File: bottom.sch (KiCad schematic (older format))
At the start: 8 parts, among them J6 FFC-0.5MM-6POS, J7 Port_3, J8 Port_4

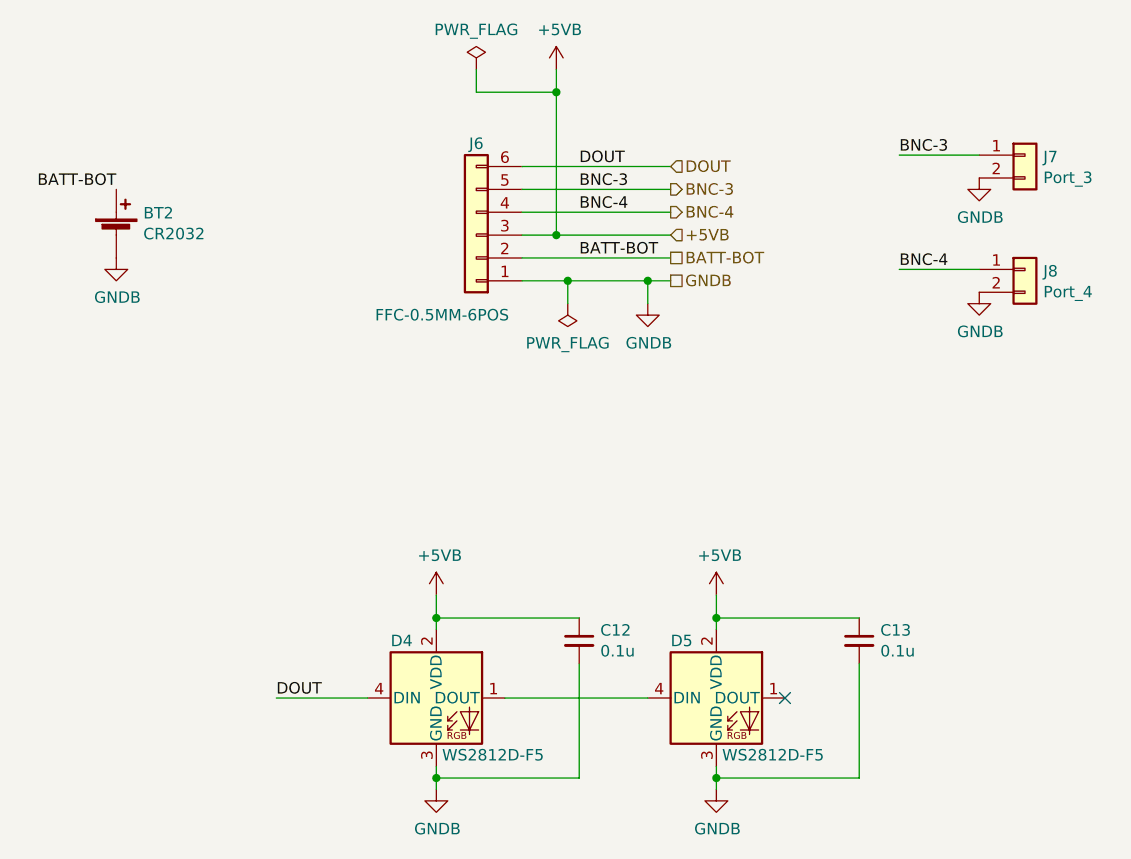
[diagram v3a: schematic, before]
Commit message: Fix: bottom FFC connector has wrong pinout
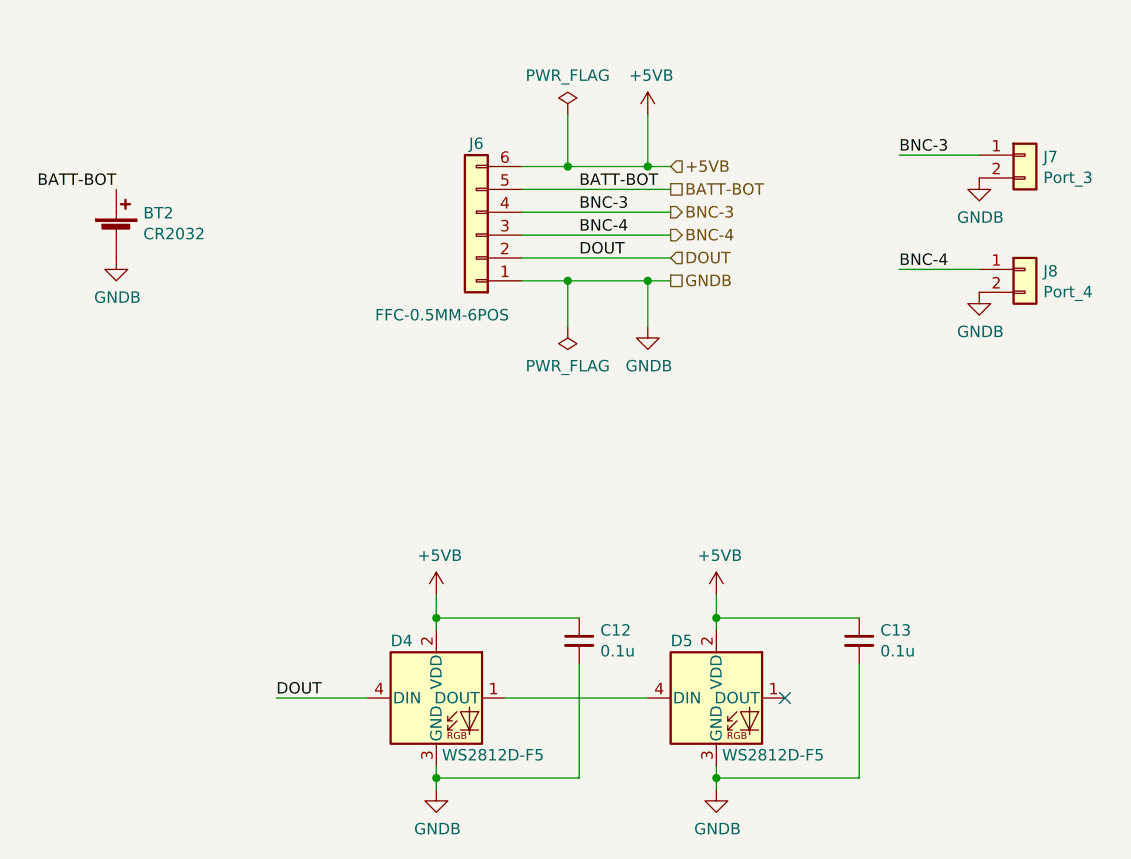
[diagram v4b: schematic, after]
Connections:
- net +5VB: now also J6.6 (Pin_6); no longer J6.3 (Pin_3)
- net BATT-BOT: now also J6.5 (Pin_5); no longer J6.2 (Pin_2)
- net BNC-3: now also J6.4 (Pin_4); no longer J6.5 (Pin_5)
- net BNC-4: now also J6.3 (Pin_3); no longer J6.4 (Pin_4)
- net DOUT: now also J6.2 (Pin_2); no longer J6.6 (Pin_6)
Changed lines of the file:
@@
 	1    0    0    -1
 $EndComp
-Text HLabel 5700 1925 2    50   Input ~ 0
-DOUT
-Text HLabel 5700 2025 2    50   Output ~ 0
-BNC-3
-Text HLabel 5700 2125 2    50   Output ~ 0
-BNC-4
-Text HLabel 5700 2325 2    50   UnSpc ~ 0
-BATT-BOT
-Text HLabel 5700 2425 2    50   UnSpc ~ 0
-GNDB
 Text Label 3275 2025 2    50   ~ 0
-BATT-BOT
-Text Label 5300 2325 0    50   ~ 0
 BATT-BOT
 $Comp
@@
 	1    0    0    -1
 $EndComp
-Text Label 5300 2125 0    50   ~ 0
-BNC-4
-Text Label 5300 2025 0    50   ~ 0
-BNC-3
-Text Label 5300 1925 0    50   ~ 0
-DOUT
 $Comp
 L Connector_Generic:Conn_01x06 J6
@@
 	-1   0    0    1
 $EndComp
-Wire Wire Line
-	5050 1925 5700 1925
-Wire Wire Line
-	5050 2025 5700 2025
-Wire Wire Line
-	5050 2125 5700 2125
-Wire Wire Line
-	5050 2325 5700 2325
 Text Label 6700 1875 0    50   ~ 0
 BNC-3
@@
 $EndComp
 $Comp
-L node:GNDB #PWR0103
-U 1 1 5CA43459
-P 5600 2525
-F 0 "#PWR0103" H 5600 2275 50  0001 C CNN
-F 1 "GNDB" H 5605 2352 50  0000 C CNN
-F 2 "" H 5600 2525 50  0001 C CNN
-F 3 "" H 5600 2525 50  0001 C CNN
-	1    5600 2525
-	1    0    0    -1
-$EndComp
-$Comp
 L node:GNDB #PWR0104
 U 1 1 5CA437BD
@@
 	1    0    0    -1
 $EndComp
-Text HLabel 5700 2225 2    50   Input ~ 0
-+5VB
 $Comp
 L node:+5VB #PWR0108
@@
 $EndComp
 $Comp
-L node:+5VB #PWR0110
-U 1 1 5CA4532B
-P 5200 1500
-F 0 "#PWR0110" H 5200 1350 50  0001 C CNN
-F 1 "+5VB" H 5215 1673 50  0000 C CNN
-F 2 "" H 5200 1500 50  0001 C CNN
-F 3 "" H 5200 1500 50  0001 C CNN
-	1    5200 1500
-	1    0    0    -1
-$EndComp
-$Comp
 L node:+5VB #PWR0109
 U 1 1 5CA03EDF
@@
 $EndComp
 Wire Wire Line
-	5200 2225 5700 2225
-Wire Wire Line
-	5050 2225 5200 2225
-Connection ~ 5200 2225
-Wire Wire Line
-	5200 1500 5200 1600
-Wire Wire Line
 	4675 3800 4675 3900
 Connection ~ 4675 3900
 Wire Wire Line
+	5250 2425 5600 2425
+Connection ~ 5250 2425
+Wire Wire Line
+	5250 2625 5250 2425
+$Comp
+L power:PWR_FLAG #FLG0102
+U 1 1 5CA09F39
+P 5250 2625
+F 0 "#FLG0102" H 5250 2700 50  0001 C CNN
+F 1 "PWR_FLAG" H 5250 2798 50  0000 C CNN
+F 2 "" H 5250 2625 50  0001 C CNN
+F 3 "~" H 5250 2625 50  0001 C CNN
+	1    5250 2625
+	-1   0    0    1
+$EndComp
+Wire Wire Line
+	5600 2425 5700 2425
+Connection ~ 5600 2425
+Wire Wire Line
+	5600 2625 5600 2425
+Wire Wire Line
 	5050 2425 5250 2425
-Wire Wire Line
-	5600 2525 5600 2425
-Connection ~ 5600 2425
-Wire Wire Line
-	5600 2425 5700 2425
+$Comp
+L node:GNDB #PWR0103
+U 1 1 5CA43459
+P 5600 2625
+F 0 "#PWR0103" H 5600 2375 50  0001 C CNN
+F 1 "GNDB" H 5605 2452 50  0000 C CNN
+F 2 "" H 5600 2625 50  0001 C CNN
+F 3 "" H 5600 2625 50  0001 C CNN
+	1    5600 2625
+	1    0    0    -1
+$EndComp
+Text HLabel 5700 2425 2    50   UnSpc ~ 0
+GNDB
+Text HLabel 5700 1925 2    50   Input ~ 0
++5VB
+Text HLabel 5700 2325 2    50   Input ~ 0
+DOUT
+Text HLabel 5700 2125 2    50   Output ~ 0
+BNC-3
+Text HLabel 5700 2225 2    50   Output ~ 0
+BNC-4
+Text HLabel 5700 2025 2    50   UnSpc ~ 0
+BATT-BOT
+Text Label 5300 2025 0    50   ~ 0
+BATT-BOT
+Text Label 5300 2225 0    50   ~ 0
+BNC-4
+Text Label 5300 2125 0    50   ~ 0
+BNC-3
+Text Label 5300 2325 0    50   ~ 0
+DOUT
+Wire Wire Line
+	5050 2325 5700 2325
+Wire Wire Line
+	5050 2125 5700 2125
+Wire Wire Line
+	5050 2225 5700 2225
+Wire Wire Line
+	5050 2025 5700 2025
+$Comp
+L node:+5VB #PWR0110
+U 1 1 5CA4532B
+P 5600 1700
+F 0 "#PWR0110" H 5600 1550 50  0001 C CNN
+F 1 "+5VB" H 5615 1873 50  0000 C CNN
+F 2 "" H 5600 1700 50  0001 C CNN
+F 3 "" H 5600 1700 50  0001 C CNN
+	1    5600 1700
+	1    0    0    -1
+$EndComp
 $Comp
 L power:PWR_FLAG #FLG0101
 U 1 1 5CA08161
-P 4850 1500
-F 0 "#FLG0101" H 4850 1575 50  0001 C CNN
-F 1 "PWR_FLAG" H 4850 1673 50  0000 C CNN
-F 2 "" H 4850 1500 50  0001 C CNN
-F 3 "~" H 4850 1500 50  0001 C CNN
-	1    4850 1500
-	1    0    0    -1
-$EndComp
-Wire Wire Line
-	4850 1500 4850 1600
-Wire Wire Line
-	4850 1600 5200 1600
-Connection ~ 5200 1600
-Wire Wire Line
-	5200 1600 5200 2225
-$Comp
-L power:PWR_FLAG #FLG0102
-U 1 1 5CA09F39
-P 5250 2525
-F 0 "#FLG0102" H 5250 2600 50  0001 C CNN
-F 1 "PWR_FLAG" H 5250 2698 50  0000 C CNN
-F 2 "" H 5250 2525 50  0001 C CNN
-F 3 "~" H 5250 2525 50  0001 C CNN
-	1    5250 2525
-	-1   0    0    1
-$EndComp
-Wire Wire Line
-	5250 2525 5250 2425
-Connection ~ 5250 2425
-Wire Wire Line
-	5250 2425 5600 2425
+P 5250 1700
+F 0 "#FLG0101" H 5250 1775 50  0001 C CNN
+F 1 "PWR_FLAG" H 5250 1873 50  0000 C CNN
+F 2 "" H 5250 1700 50  0001 C CNN
+F 3 "~" H 5250 1700 50  0001 C CNN
+	1    5250 1700
+	1    0    0    -1
+$EndComp
+Wire Wire Line
+	5600 1700 5600 1925
+Connection ~ 5600 1925
+Wire Wire Line
+	5600 1925 5700 1925
+Wire Wire Line
+	5050 1925 5250 1925
+Wire Wire Line
+	5250 1700 5250 1925
+Connection ~ 5250 1925
+Wire Wire Line
+	5250 1925 5600 1925
 $EndSCHEMATC

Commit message: Update entries for Seeed BOM
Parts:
- BT2: MPN BK-912 -> (none)
- J7, J8: MPN (none) -> 0530470210
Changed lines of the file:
@@
 F 2 "gsg-modules:BK-912" V 3275 2285 50  0001 C CNN
 F 3 "http://www.memoryprotectiondevices.com/datasheets/BK-912-datasheet.pdf" V 3275 2285 50  0001 C CNN
-F 4 "BK-912" H 1475 -225 50  0001 C CNN "MPN"
-F 5 "1" H 1475 -225 50  0001 C CNN "Min Quantity"
+F 4 "1" H 1475 -225 50  0001 C CNN "Min Quantity"
 	1    3275 2225
 	1    0    0    -1
@@
 F 2 "Connector_Molex:Molex_PicoBlade_53047-0210_1x02_P1.25mm_Vertical" H 7250 1875 50  0001 C CNN
 F 3 "~" H 7250 1875 50  0001 C CNN
+F 4 "0530470210" H 7250 1875 50  0001 C CNN "MPN"
 	1    7250 1875
 	1    0    0    -1
@@
 F 2 "Connector_Molex:Molex_PicoBlade_53047-0210_1x02_P1.25mm_Vertical" H 7250 2375 50  0001 C CNN
 F 3 "~" H 7250 2375 50  0001 C CNN
+F 4 "0530470210" H 7250 2375 50  0001 C CNN "MPN"
 	1    7250 2375
 	1    0    0    -1
